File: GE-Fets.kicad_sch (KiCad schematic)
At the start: 14 parts, among them Q1 YJG150N03A, Q4 YJG150N03A, U4 INA185A

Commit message: switched to stm32
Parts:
- U4: value INA185A -> INA185A1
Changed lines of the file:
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@@
       (effects (font (size 1.27 1.27)) hide)
     )
-    (property "Datasheet" "~" (id 3) (at 227.33 72.39 0)
+    (property "Datasheet" "" (id 3) (at 227.33 72.39 0)
       (effects (font (size 1.27 1.27)) hide)
     )
@@
       (effects (font (size 1.27 1.27)) hide)
     )
-    (property "Datasheet" "~" (id 3) (at 227.33 85.09 0)
+    (property "Datasheet" "" (id 3) (at 227.33 85.09 0)
       (effects (font (size 1.27 1.27)) hide)
     )
@@
     (in_bom yes) (on_board yes) (fields_autoplaced)
     (property "Reference" "U4" (id 0) (at 214.63 81.915 0))
-    (property "Value" "INA185A" (id 1) (at 214.63 84.455 0))
+    (property "Value" "INA185A1" (id 1) (at 214.63 84.455 0))
     (property "Footprint" "Package_TO_SOT_SMD:SOT-563" (id 2) (at 198.12 55.88 0)
       (effects (font (size 1.27 1.27)) hide)
     )
-    (property "Datasheet" "https://www.mouser.com/ProductDetail/Texas-Instruments/INA185A2IDRLT?qs=vLWxofP3U2xrYvja0PA2yg%3D%3D" (id 3) (at 198.12 55.88 0)
+    (property "Datasheet" "https://www.digikey.com/en/products/detail/texas-instruments/INA185A1IDRLR/10448282" (id 3) (at 198.12 55.88 0)
       (effects (font (size 1.27 1.27)) hide)
     )

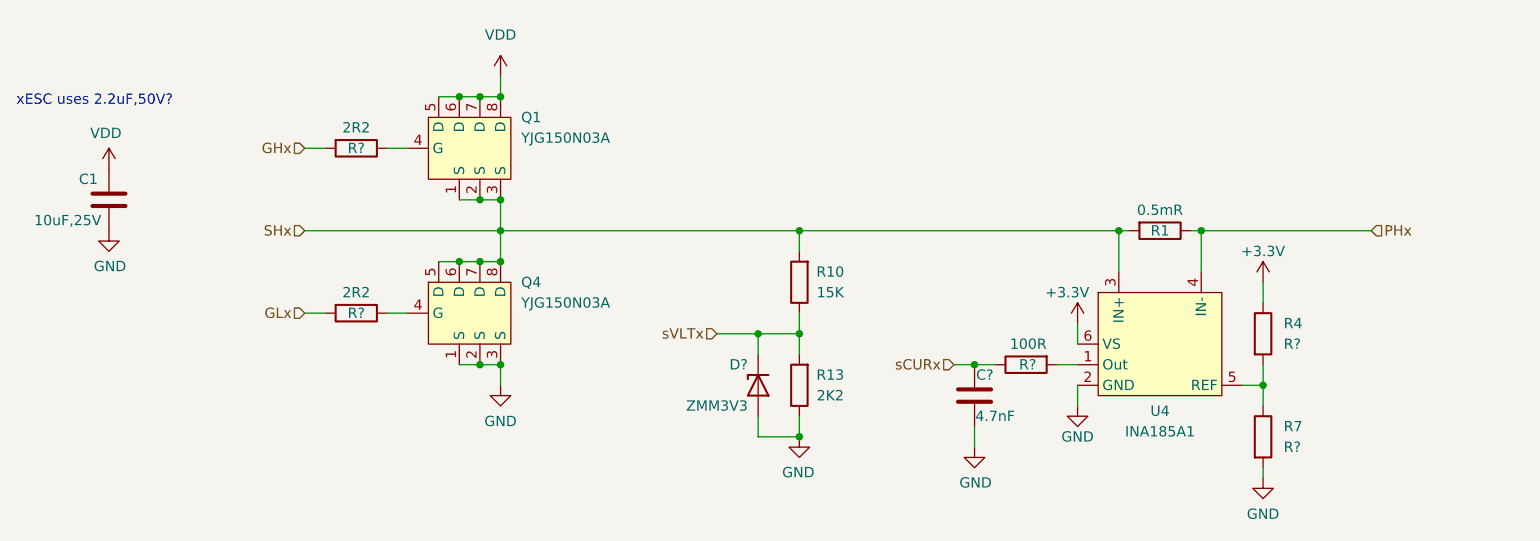
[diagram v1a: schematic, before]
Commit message: moved the Dsub off-board, most of initial layout routed
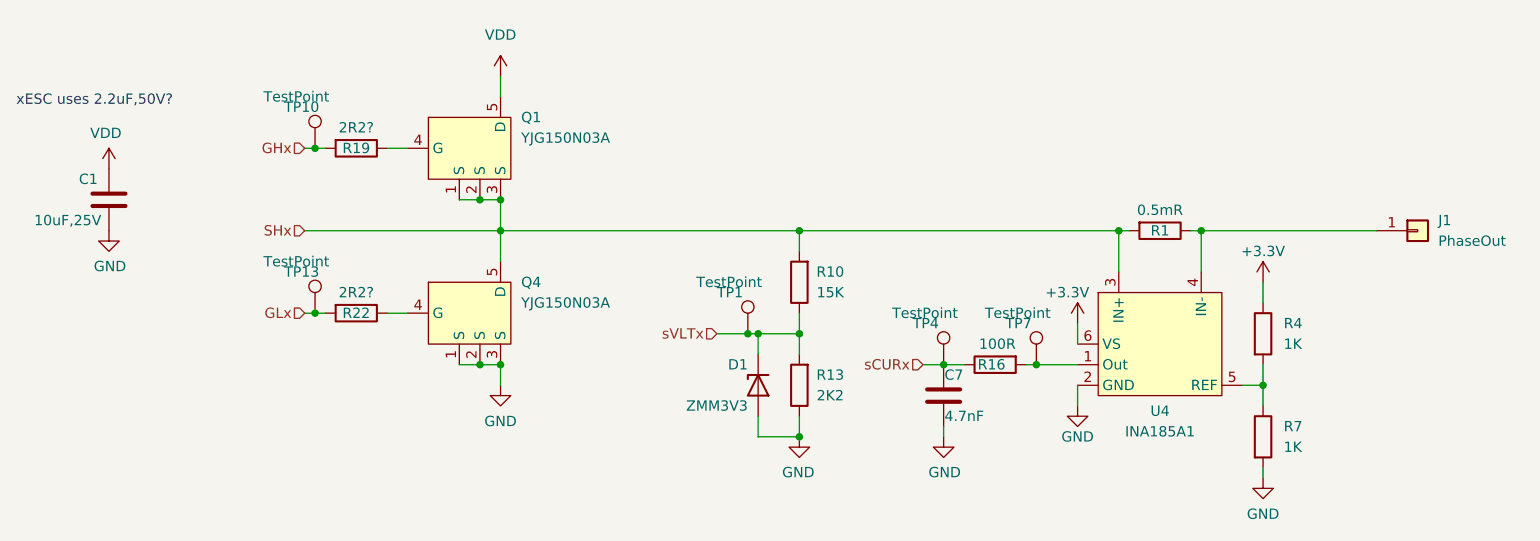
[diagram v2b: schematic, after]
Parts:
- added J1: PhaseOut, AlfredoFootprints:TGD_ESC_PwrPad, symbol Connector_Generic:Conn_01x01
- added TP1, TP10, TP13, TP4, TP7: TestPoint, AlfredoFootprints:GE_TestPoint_Loop, symbol Connector:TestPoint
- R1: LCSC (none) -> ?
- R19, R22: renamed from R?; value 2R2 -> 2R2?
- R4, R7: value R? -> 1K; LCSC (none) -> ?
- gave numbers to parts that had none: 3
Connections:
- net GHx: now also TP10.1
- net GLx: now also TP13.1
- net SHx: no longer Q4.6 (D), Q4.7 (D), Q4.8 (D)
- net VDD: no longer Q1.6 (D), Q1.7 (D), Q1.8 (D)
- net sCURx: now also TP4.1
- net sVLTx: now also TP1.1
- net at R16.2, U4.1 (Out): now also TP7.1
- net PHx: no longer names the net of R1.1, U4.4 (IN-)
- net PHx: now also J1.1 (Pin_1)
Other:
- moved on the sheet: C7, R16

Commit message: Updated BOM
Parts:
- R1: LCSC ? -> C710261
- R19, R22: value 2R2? -> 15R; LCSC C22809 -> C22810
- R4, R7: LCSC ? -> C21190
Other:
- note added: "gate resitors can be as low as 3.6 ohms?"
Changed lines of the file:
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@@
     (stroke (width 0) (type default) (color 0 0 0 0))
+  )
+  (text "gate resitors can be as low as 3.6 ohms?" (at 83.82 35.56 0)
+    (effects (font (size 1.27 1.27)) (justify left bottom))
   )
   (text "xESC uses 2.2uF,50V?" (at 73.66 44.45 0)
@@
     (in_bom yes) (on_board yes)
     (property "Reference" "R19" (id 0) (at 115.57 49.53 90))
-    (property "Value" "2R2?" (id 1) (at 115.57 46.99 90))
+    (property "Value" "15R" (id 1) (at 115.57 46.99 90))
     (property "Footprint" "Resistor_SMD:R_0603_1608Metric" (id 2) (at 115.57 47.752 90)
       (effects (font (size 1.27 1.27)) hide)
     )
-    (property "Datasheet" "https://lcsc.com/product-detail/Chip-Resistor-Surface-Mount_UNI-ROYAL-Uniroyal-Elec-0603WAF1502T5E_C22809.html" (id 3) (at 115.57 49.53 0)
-      (effects (font (size 1.27 1.27)) hide)
-    )
-    (property "LCSC" "C22809" (id 4) (at 115.57 49.53 0)
+    (property "Datasheet" "https://lcsc.com/product-detail/Chip-Resistor-Surface-Mount_UNI-ROYAL-Uniroyal-Elec-0603WAF150JT5E_C22810.html" (id 3) (at 115.57 49.53 0)
+      (effects (font (size 1.27 1.27)) hide)
+    )
+    (property "LCSC" "C22810" (id 4) (at 115.57 49.53 0)
       (effects (font (size 1.27 1.27)) hide)
     )
@@
       (effects (font (size 1.27 1.27)) hide)
     )
+    (property "LCSC" "~" (id 4) (at 110.49 49.53 0)
+      (effects (font (size 1.27 1.27)) hide)
+    )
     (pin "1")
   )
@@
     )
     (property "Datasheet" "~" (id 3) (at 115.57 69.85 0)
+      (effects (font (size 1.27 1.27)) hide)
+    )
+    (property "LCSC" "~" (id 4) (at 110.49 69.85 0)
       (effects (font (size 1.27 1.27)) hide)
     )
@@
       (effects (font (size 1.27 1.27)) hide)
     )
+    (property "LCSC" "~" (id 4) (at 199.39 76.2 0)
+      (effects (font (size 1.27 1.27)) hide)
+    )
     (pin "1")
   )
@@
       (effects (font (size 1.27 1.27)) hide)
     )
+    (property "LCSC" "~" (id 4) (at 163.83 72.39 0)
+      (effects (font (size 1.27 1.27)) hide)
+    )
     (pin "1")
   )
@@
     (in_bom yes) (on_board yes)
     (property "Reference" "R22" (id 0) (at 115.57 69.85 90))
-    (property "Value" "2R2?" (id 1) (at 115.57 67.31 90))
+    (property "Value" "15R" (id 1) (at 115.57 67.31 90))
     (property "Footprint" "Resistor_SMD:R_0603_1608Metric" (id 2) (at 115.57 68.072 90)
       (effects (font (size 1.27 1.27)) hide)
     )
-    (property "Datasheet" "https://lcsc.com/product-detail/Chip-Resistor-Surface-Mount_UNI-ROYAL-Uniroyal-Elec-0603WAF1502T5E_C22809.html" (id 3) (at 115.57 69.85 0)
-      (effects (font (size 1.27 1.27)) hide)
-    )
-    (property "LCSC" "C22809" (id 4) (at 115.57 69.85 0)
+    (property "Datasheet" "https://lcsc.com/product-detail/Chip-Resistor-Surface-Mount_UNI-ROYAL-Uniroyal-Elec-0603WAF150JT5E_C22810.html" (id 3) (at 115.57 69.85 0)
+      (effects (font (size 1.27 1.27)) hide)
+    )
+    (property "LCSC" "C22810" (id 4) (at 115.57 69.85 0)
       (effects (font (size 1.27 1.27)) hide)
     )
@@
       (effects (font (size 1.27 1.27)) hide)
     )
-    (property "LCSC" "?" (id 4) (at 214.63 59.69 0)
+    (property "LCSC" "C710261" (id 4) (at 214.63 59.69 0)
       (effects (font (size 1.27 1.27)) hide)
     )
@@
       (effects (font (size 1.27 1.27)) hide)
     )
-    (property "Datasheet" "?" (id 3) (at 227.33 72.39 0)
-      (effects (font (size 1.27 1.27)) hide)
-    )
-    (property "LCSC" "?" (id 4) (at 227.33 72.39 0)
+    (property "Datasheet" "https://lcsc.com/product-detail/Chip-span-style-background-color-ff0-Resistor-span-Surface-Mount_UNI-ROYAL-Uniroyal-Elec-0603WAF1001T5E_C21190.html" (id 3) (at 227.33 72.39 0)
+      (effects (font (size 1.27 1.27)) hide)
+    )
+    (property "LCSC" "C21190" (id 4) (at 227.33 72.39 0)
       (effects (font (size 1.27 1.27)) hide)
     )
@@
       (effects (font (size 1.27 1.27)) hide)
     )
+    (property "LCSC" "~" (id 4) (at 187.96 76.2 0)
+      (effects (font (size 1.27 1.27)) hide)
+    )
     (pin "1")
   )
@@
       (effects (font (size 1.27 1.27)) hide)
     )
-    (property "Datasheet" "?" (id 3) (at 227.33 85.09 0)
-      (effects (font (size 1.27 1.27)) hide)
-    )
-    (property "LCSC" "?" (id 4) (at 227.33 85.09 0)
-      (effects (font (size 1.27 1.27)) hide)
-    )
+    (property "Datasheet" "https://lcsc.com/product-detail/Chip-span-style-background-color-ff0-Resistor-span-Surface-Mount_UNI-ROYAL-Uniroyal-Elec-0603WAF1001T5E_C21190.html" (id 3) (at 227.33 85.09 0)
+      (effects (font (size 1.27 1.27)) hide)
+    )
+    (property "LCSC" "C21190" (id 4) (at 227.33 85.09 0)
+      (effects (font (size 1.27 1.27)) hide)
+    )

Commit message: major schematic and pcb changes for production ready prototype
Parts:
- removed R4, R7: 1K, Resistor_SMD:R_0603_1608Metric, symbol Device:R
- removed TP1, TP10, TP13, TP4, TP7: TestPoint, AlfredoFootprints:GE_TestPoint_Loop, symbol Connector:TestPoint
- C1: value 10uF,25V -> 10uF,50V; footprint Capacitor_SMD:C_0805_2012Metric -> Capacitor_SMD:C_1206_3216Metric; LCSC C15850 -> C13585
- C7: footprint Capacitor_SMD:C_0603_1608Metric -> Capacitor_SMD:C_0402_1005Metric; LCSC C53987 -> (none)
- D1: value ZMM3V3 -> B3V3; footprint Diode_SMD:D_MiniMELF -> Diode_SMD:D_SOD-323_HandSoldering; LCSC C8056 -> C173439
- J1: footprint AlfredoFootprints:TGD_ESC_PwrPad -> AlfredoFootprints:GE_PwrPad1
- R10: footprint Resistor_SMD:R_0603_1608Metric -> Resistor_SMD:R_0402_1005Metric; LCSC C22809 -> (none)
- R13: footprint Resistor_SMD:R_0603_1608Metric -> Resistor_SMD:R_0402_1005Metric; LCSC C4190 -> (none)
- R16: footprint Resistor_SMD:R_0603_1608Metric -> Resistor_SMD:R_0402_1005Metric; LCSC C22775 -> (none)
- R19, R22: footprint Resistor_SMD:R_0603_1608Metric -> Resistor_SMD:R_0402_1005Metric; LCSC C22810 -> (none)
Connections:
- net REF_1V65: now reaches U4.5 (REF)

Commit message: First rev of layout before routing
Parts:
- C1: value 10uF,50V -> 4.7uF,50V; LCSC C13585 -> (none)
- C7: LCSC (none) -> C1538
- D1: value B3V3 -> Z3V3; LCSC C173439 -> C75073
- R19: value 15R -> 2.2R
- R22: value 15R -> 0R
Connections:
- net +3V3 renamed +5V
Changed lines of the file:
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@@
     (in_bom yes) (on_board yes)
     (property "Reference" "R19" (id 0) (at 115.57 49.53 90))
-    (property "Value" "15R" (id 1) (at 115.57 46.99 90))
+    (property "Value" "2.2R" (id 1) (at 115.57 46.99 90))
     (property "Footprint" "Resistor_SMD:R_0402_1005Metric" (id 2) (at 115.57 47.752 90)
       (effects (font (size 1.27 1.27)) hide)
@@
       (effects (font (size 1.27 1.27)) (justify left))
     )
-    (property "Value" "B3V3" (id 1) (at 163.83 81.28 90)
+    (property "Value" "Z3V3" (id 1) (at 163.83 81.28 90)
       (effects (font (size 1.27 1.27)) (justify left))
     )
@@
       (effects (font (size 1.27 1.27)) hide)
     )
-    (property "Datasheet" "https://lcsc.com/product-detail/Zener-Diodes_MDD%EF%BC%88Microdiode-Electronics%EF%BC%89-MDD%EF%BC%88Microdiode-Electronics%EF%BC%89-BZT52C3V3S_C173439.html" (id 3) (at 165.1 78.74 0)
-      (effects (font (size 1.27 1.27)) hide)
-    )
-    (property "LCSC" "C173439" (id 4) (at 165.1 78.74 0)
+    (property "Datasheet" "https://lcsc.com/product-detail/Zener-Diodes_onsemi-onsemi-MM3Z3V3T1G_C75073.html" (id 3) (at 165.1 78.74 0)
+      (effects (font (size 1.27 1.27)) hide)
+    )
+    (property "LCSC" "C75073" (id 4) (at 165.1 78.74 0)
       (effects (font (size 1.27 1.27)) hide)
     )
@@
       (effects (font (size 1.27 1.27)) hide)
     )
-    (property "Datasheet" "" (id 3) (at 187.96 80.01 0)
-      (effects (font (size 1.27 1.27)) hide)
-    )
-    (property "LCSC" "" (id 4) (at 187.96 80.01 0)
-      (effects (font (size 1.27 1.27)) hide)
-    )
-    (pin "1")
-    (pin "2")
+    (property "Datasheet" "https://lcsc.com/product-detail/Multilayer-Ceramic-Capacitors-MLCC---SMD-SMT_FHGuangdong-Fenghua-Advanced-Tech-FHGuangdong-Fenghua-Advanced-Tech-0402B472K500NT_C1538.html" (id 3) (at 187.96 80.01 0)
+      (effects (font (size 1.27 1.27)) hide)
+    )
+    (property "LCSC" "C1538" (id 4) (at 187.96 80.01 0)
+      (effects (font (size 1.27 1.27)) hide)
+    )
+    (pin "1")
+    (pin "2")
+  )
+  (symbol (lib_id "power:+5V") (at 204.47 71.12 0) (unit 1)
+    (in_bom yes) (on_board yes) (fields_autoplaced)
+    (property "Reference" "#PWR0112" (id 0) (at 204.47 74.93 0)
+      (effects (font (size 1.27 1.27)) hide)
+    )
+    (property "Value" "+5V" (id 1) (at 204.47 66.04 0))
+    (property "Footprint" "" (id 2) (at 204.47 71.12 0)
+      (effects (font (size 1.27 1.27)) hide)
+    )
+    (property "Datasheet" "" (id 3) (at 204.47 71.12 0)
+      (effects (font (size 1.27 1.27)) hide)
+    )
+    (pin "1")
   )
   (symbol (lib_id "Device:R") (at 170.18 66.04 180) (unit 1)
@@
     (in_bom yes) (on_board yes)
     (property "Reference" "R22" (id 0) (at 115.57 69.85 90))
-    (property "Value" "15R" (id 1) (at 115.57 67.31 90))
+    (property "Value" "0R" (id 1) (at 115.57 67.31 90))
     (property "Footprint" "Resistor_SMD:R_0402_1005Metric" (id 2) (at 115.57 68.072 90)
       (effects (font (size 1.27 1.27)) hide)
@@
     (in_bom yes) (on_board yes)
     (property "Reference" "C1" (id 0) (at 82.55 53.34 0))
-    (property "Value" "10uF,50V" (id 1) (at 80.01 58.42 0))
+    (property "Value" "4.7uF,50V" (id 1) (at 80.01 58.42 0))
     (property "Footprint" "Capacitor_SMD:C_1206_3216Metric" (id 2) (at 86.0552 59.69 0)
       (effects (font (size 1.27 1.27)) hide)
     )
-    (property "Datasheet" "https://lcsc.com/product-detail/null_C13585.html" (id 3) (at 85.09 55.88 0)
-      (effects (font (size 1.27 1.27)) hide)
-    )
-    (property "LCSC" "C13585" (id 4) (at 85.09 55.88 0)
+    (property "Datasheet" "" (id 3) (at 85.09 55.88 0)
+      (effects (font (size 1.27 1.27)) hide)
+    )
+    (property "LCSC" "" (id 4) (at 85.09 55.88 0)
       (effects (font (size 1.27 1.27)) hide)
     )
@@
       (effects (font (size 1.27 1.27)) hide)
     )
-    (pin "1")
-  )
-  (symbol (lib_id "power:+3.3V") (at 204.47 71.12 0) (unit 1)
-    (in_bom yes) (on_board yes)
-    (property "Reference" "#PWR0113" (id 0) (at 204.47 74.93 0)
-      (effects (font (size 1.27 1.27)) hide)
-    )
-    (property "Value" "+3.3V" (id 1) (at 203.2 67.31 0))
-    (property "Footprint" "" (id 2) (at 204.47 71.12 0)
-      (effects (font (size 1.27 1.27)) hide)
-    )
-    (property "Datasheet" "" (id 3) (at 204.47 71.12 0)
-      (effects (font (size 1.27 1.27)) hide)
-    )

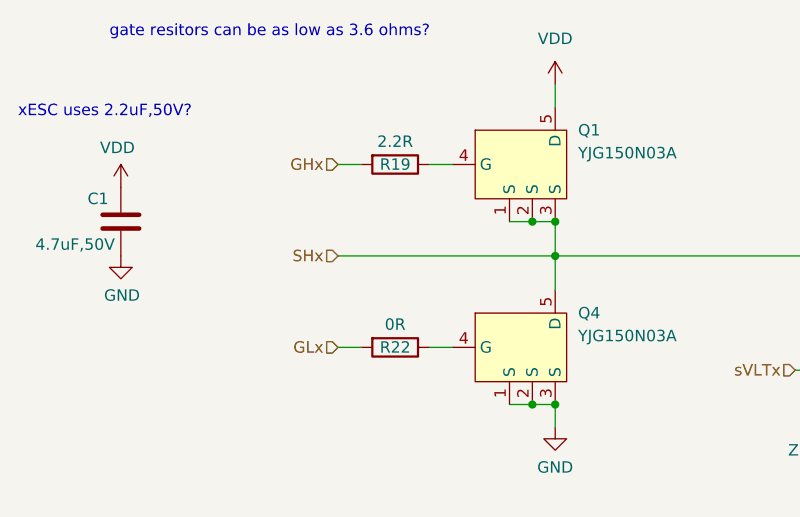
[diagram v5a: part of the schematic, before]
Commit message: all nets routed for next revision, no major drc errors
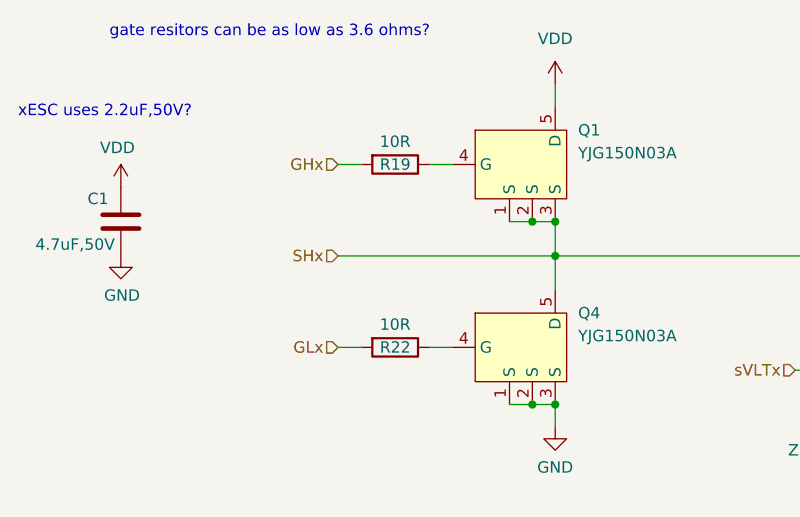
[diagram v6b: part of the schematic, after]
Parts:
- C1: LCSC (none) -> C29823
- R1: footprint Resistor_SMD:R_2512_6332Metric -> AlfredoFootprints:GE_R_2512
- R10: LCSC (none) -> C25756
- R13: LCSC (none) -> C25879
- R16: LCSC (none) -> C25076
- R19: value 2.2R -> 10R; LCSC (none) -> C25077
- R22: value 0R -> 10R; LCSC (none) -> C25077
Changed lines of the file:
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@@
     (in_bom yes) (on_board yes)
     (property "Reference" "R19" (id 0) (at 115.57 49.53 90))
-    (property "Value" "2.2R" (id 1) (at 115.57 46.99 90))
+    (property "Value" "10R" (id 1) (at 115.57 46.99 90))
     (property "Footprint" "Resistor_SMD:R_0402_1005Metric" (id 2) (at 115.57 47.752 90)
       (effects (font (size 1.27 1.27)) hide)
@@
       (effects (font (size 1.27 1.27)) hide)
     )
-    (property "LCSC" "" (id 4) (at 115.57 49.53 0)
+    (property "LCSC" "C25077" (id 4) (at 115.57 49.53 0)
       (effects (font (size 1.27 1.27)) hide)
     )
@@
       (effects (font (size 1.27 1.27)) hide)
     )
-    (property "LCSC" "" (id 4) (at 194.31 76.2 0)
+    (property "LCSC" "C25076" (id 4) (at 194.31 76.2 0)
       (effects (font (size 1.27 1.27)) hide)
     )
@@
       (effects (font (size 1.27 1.27)) hide)
     )
-    (property "LCSC" "" (id 4) (at 170.18 66.04 0)
+    (property "LCSC" "C25756" (id 4) (at 170.18 66.04 0)
       (effects (font (size 1.27 1.27)) hide)
     )
@@
     (in_bom yes) (on_board yes)
     (property "Reference" "R22" (id 0) (at 115.57 69.85 90))
-    (property "Value" "0R" (id 1) (at 115.57 67.31 90))
+    (property "Value" "10R" (id 1) (at 115.57 67.31 90))
     (property "Footprint" "Resistor_SMD:R_0402_1005Metric" (id 2) (at 115.57 68.072 90)
       (effects (font (size 1.27 1.27)) hide)
@@
       (effects (font (size 1.27 1.27)) hide)
     )
-    (property "LCSC" "" (id 4) (at 115.57 69.85 0)
+    (property "LCSC" "C25077" (id 4) (at 115.57 69.85 0)
       (effects (font (size 1.27 1.27)) hide)
     )
@@
     (property "Reference" "R1" (id 0) (at 214.63 59.69 90))
     (property "Value" "0.5mR" (id 1) (at 214.63 57.15 90))
-    (property "Footprint" "Resistor_SMD:R_2512_6332Metric" (id 2) (at 214.63 57.912 90)
+    (property "Footprint" "AlfredoFootprints:GE_R_2512" (id 2) (at 214.63 57.912 90)
       (effects (font (size 1.27 1.27)) hide)
     )
@@
       (effects (font (size 1.27 1.27)) hide)
     )
-    (property "Datasheet" "" (id 3) (at 85.09 55.88 0)
-      (effects (font (size 1.27 1.27)) hide)
-    )
-    (property "LCSC" "" (id 4) (at 85.09 55.88 0)
+    (property "Datasheet" "https://lcsc.com/product-detail/Multilayer-Ceramic-Capacitors-MLCC---SMD-SMT_FHGuangdong-Fenghua-Advanced-Tech-FHGuangdong-Fenghua-Advanced-Tech-1206B475K500NT_C29823.html" (id 3) (at 85.09 55.88 0)
+      (effects (font (size 1.27 1.27)) hide)
+    )
+    (property "LCSC" "C29823" (id 4) (at 85.09 55.88 0)
       (effects (font (size 1.27 1.27)) hide)
     )
@@
       (effects (font (size 1.27 1.27)) hide)
     )
-    (property "LCSC" "" (id 4) (at 170.18 78.74 0)
-      (effects (font (size 1.27 1.27)) hide)
-    )
+    (property "LCSC" "C25879" (id 4) (at 170.18 78.74 0)
+      (effects (font (size 1.27 1.27)) hide)
+    )
